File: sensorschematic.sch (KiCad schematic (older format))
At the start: 6 parts, among them J1 Conn_01x03_Male, U1 LM35DZ_NOPB

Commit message: Updated Parts
Updated parts to components that are available for order rather than obsolete, out-of-stock, or non-real components.
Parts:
- removed C1, C2: C, symbol pspice:C
- removed C3: 1uF, symbol pspice:C
- removed R1: 75, symbol Device:R_US
- added C1: CL21B474KOFNNNE, CAP_CL21_SAM, symbol CL21B474KOFNNNE:CL21B474KOFNNNE
- added C2: 04025C101KAT2A, 0402_AVX, symbol 04025C101KAT2A:04025C101KAT2A
- added C3: CL05A105KO5NNNC, CAP_CL05_SAM, symbol CL05A105KO5NNNC:CL05A105KO5NNNC
- added R1: CR0603-FX-75R0ELF, BO_CR0603, symbol CR0603-FX-75R0ELF:CR0603-FX-75R0ELF
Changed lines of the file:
@@
 $EndDescr
-$Comp
-L pspice:C C1
-U 1 1 60F31FB8
-P 2000 3300
-AR Path="/5EA98F1B/60F31FB8" Ref="C1"  Part="1"
-AR Path="/60B9480C/60F31FB8" Ref="C4"  Part="1"
-AR Path="/60B94B7E/60F31FB8" Ref="C7"  Part="1"
-AR Path="/60B95D06/60F31FB8" Ref="C10"  Part="1"
-AR Path="/60B95D0B/60F31FB8" Ref="C13"  Part="1"
-AR Path="/60B95D10/60F31FB8" Ref="C16"  Part="1"
-AR Path="/60B99A53/60F31FB8" Ref="C19"  Part="1"
-AR Path="/60B99A58/60F31FB8" Ref="C22"  Part="1"
-AR Path="/60B99A5D/60F31FB8" Ref="C25"  Part="1"
-AR Path="/60B99A62/60F31FB8" Ref="C28"  Part="1"
-AR Path="/60B99A67/60F31FB8" Ref="C31"  Part="1"
-AR Path="/60B99A6C/60F31FB8" Ref="C34"  Part="1"
-F 0 "C34" H 2178 3391 50  0000 L CNN
-F 1 "C" H 2178 3346 50  0001 L CNN
-F 2 "" H 2000 3300 50  0001 C CNN
-F 3 "~" H 2000 3300 50  0001 C CNN
-F 4 "C" H 2000 3300 50  0001 C CNN "Spice_Primitive"
-F 5 ".47u" H 2178 3300 50  0000 L CNN "Spice_Model"
-F 6 "Y" H 2000 3300 50  0001 C CNN "Spice_Netlist_Enabled"
-F 7 "16V" H 2178 3209 50  0000 L CNN "Vmax"
-	1    2000 3300
-	1    0    0    -1
-$EndComp
-$Comp
-L pspice:C C2
-U 1 1 60F3306C
-P 2600 3300
-AR Path="/5EA98F1B/60F3306C" Ref="C2"  Part="1"
-AR Path="/60B9480C/60F3306C" Ref="C5"  Part="1"
-AR Path="/60B94B7E/60F3306C" Ref="C8"  Part="1"
-AR Path="/60B95D06/60F3306C" Ref="C11"  Part="1"
-AR Path="/60B95D0B/60F3306C" Ref="C14"  Part="1"
-AR Path="/60B95D10/60F3306C" Ref="C17"  Part="1"
-AR Path="/60B99A53/60F3306C" Ref="C20"  Part="1"
-AR Path="/60B99A58/60F3306C" Ref="C23"  Part="1"
-AR Path="/60B99A5D/60F3306C" Ref="C26"  Part="1"
-AR Path="/60B99A62/60F3306C" Ref="C29"  Part="1"
-AR Path="/60B99A67/60F3306C" Ref="C32"  Part="1"
-AR Path="/60B99A6C/60F3306C" Ref="C35"  Part="1"
-F 0 "C35" H 2778 3391 50  0000 L CNN
-F 1 "C" H 2778 3300 50  0001 L CNN
-F 2 "" H 2600 3300 50  0001 C CNN
-F 3 "~" H 2600 3300 50  0001 C CNN
-F 4 "C" H 2600 3300 50  0001 C CNN "Spice_Primitive"
-F 5 "100p" H 2778 3300 50  0000 L CNN "Spice_Model"
-F 6 "Y" H 2600 3300 50  0001 C CNN "Spice_Netlist_Enabled"
-F 7 "50V" H 2778 3209 50  0000 L CNN "Vmax"
-	1    2600 3300
-	1    0    0    -1
-$EndComp
-$Comp
-L pspice:C C3
-U 1 1 60F35AED
-P 5100 4500
-AR Path="/5EA98F1B/60F35AED" Ref="C3"  Part="1"
-AR Path="/60B9480C/60F35AED" Ref="C6"  Part="1"
-AR Path="/60B94B7E/60F35AED" Ref="C9"  Part="1"
-AR Path="/60B95D06/60F35AED" Ref="C12"  Part="1"
-AR Path="/60B95D0B/60F35AED" Ref="C15"  Part="1"
-AR Path="/60B95D10/60F35AED" Ref="C18"  Part="1"
-AR Path="/60B99A53/60F35AED" Ref="C21"  Part="1"
-AR Path="/60B99A58/60F35AED" Ref="C24"  Part="1"
-AR Path="/60B99A5D/60F35AED" Ref="C27"  Part="1"
-AR Path="/60B99A62/60F35AED" Ref="C30"  Part="1"
-AR Path="/60B99A67/60F35AED" Ref="C33"  Part="1"
-AR Path="/60B99A6C/60F35AED" Ref="C36"  Part="1"
-F 0 "C36" H 5278 4546 50  0000 L CNN
-F 1 "1uF" H 5278 4455 50  0001 L CNN
-F 2 "" H 5100 4500 50  0001 C CNN
-F 3 "~" H 5100 4500 50  0001 C CNN
-F 4 "C" H 5100 4500 50  0001 C CNN "Spice_Primitive"
-F 5 "1u" H 5278 4455 50  0000 L CNN "Spice_Model"
-F 6 "Y" H 5100 4500 50  0001 C CNN "Spice_Netlist_Enabled"
-	1    5100 4500
-	1    0    0    -1
-$EndComp
-$Comp
-L Device:R_US R1
-U 1 1 60F37AD0
-P 5100 3900
-AR Path="/5EA98F1B/60F37AD0" Ref="R1"  Part="1"
-AR Path="/60B9480C/60F37AD0" Ref="R2"  Part="1"
-AR Path="/60B94B7E/60F37AD0" Ref="R3"  Part="1"
-AR Path="/60B95D06/60F37AD0" Ref="R4"  Part="1"
-AR Path="/60B95D0B/60F37AD0" Ref="R5"  Part="1"
-AR Path="/60B95D10/60F37AD0" Ref="R6"  Part="1"
-AR Path="/60B99A53/60F37AD0" Ref="R7"  Part="1"
-AR Path="/60B99A58/60F37AD0" Ref="R8"  Part="1"
-AR Path="/60B99A5D/60F37AD0" Ref="R9"  Part="1"
-AR Path="/60B99A62/60F37AD0" Ref="R10"  Part="1"
-AR Path="/60B99A67/60F37AD0" Ref="R11"  Part="1"
-AR Path="/60B99A6C/60F37AD0" Ref="R12"  Part="1"
-F 0 "R12" H 5168 3946 50  0000 L CNN
-F 1 "75" H 5168 3855 50  0001 L CNN
-F 2 "" V 5140 3890 50  0001 C CNN
-F 3 "~" H 5100 3900 50  0001 C CNN
-F 4 "R" H 5100 3900 50  0001 C CNN "Spice_Primitive"
-F 5 "75" H 5168 3855 50  0000 L CNN "Spice_Model"
-F 6 "Y" H 5100 3900 50  0001 C CNN "Spice_Netlist_Enabled"
-	1    5100 3900
-	1    0    0    -1
-$EndComp
 $Comp
 L Connector:Conn_01x03_Male J1
@@
 	6200 3200 5900 3200
 Wire Wire Line
-	2600 2750 2600 3050
-Wire Wire Line
 	2600 2750 2000 2750
 Wire Wire Line
-	2000 2750 2000 3050
-Wire Wire Line
-	6200 3300 5100 3300
-Wire Wire Line
-	5100 3300 5100 3750
-Wire Wire Line
 	5900 2750 5900 3200
-Wire Wire Line
-	5100 4050 5100 4250
 $Comp
 L power:GNDREF #PWR01
@@
 Wire Wire Line
 	6000 3400 6000 3800
-Wire Wire Line
-	5100 4750 5100 4950
-Wire Wire Line
-	2600 3550 2600 3750
-Wire Wire Line
-	2000 3550 2000 3800
 Text Label 5900 2750 0    50   ~ 0
 Vs
@@
 Wire Wire Line
 	4900 3500 4900 3300
-Wire Wire Line
-	4900 3300 5100 3300
-Connection ~ 5100 3300
 Wire Wire Line
 	4100 4250 4100 4550
@@
 	1    0    0    -1
 $EndComp
+$Comp
+L CL05A105KO5NNNC:CL05A105KO5NNNC C3
+U 1 1 6141E476
+P 5100 4350
+AR Path="/5EA98F1B/6141E476" Ref="C3"  Part="1"
+AR Path="/60B9480C/6141E476" Ref="C6"  Part="1"
+AR Path="/60B94B7E/6141E476" Ref="C9"  Part="1"
+AR Path="/60B95D06/6141E476" Ref="C12"  Part="1"
+AR Path="/60B95D0B/6141E476" Ref="C15"  Part="1"
+AR Path="/60B95D10/6141E476" Ref="C18"  Part="1"
+AR Path="/60B99A53/6141E476" Ref="C21"  Part="1"
+AR Path="/60B99A58/6141E476" Ref="C24"  Part="1"
+AR Path="/60B99A5D/6141E476" Ref="C27"  Part="1"
+AR Path="/60B99A62/6141E476" Ref="C30"  Part="1"
+AR Path="/60B99A67/6141E476" Ref="C33"  Part="1"
+AR Path="/60B99A6C/6141E476" Ref="C36"  Part="1"
+F 0 "C36" V 5197 4454 60  0000 L CNN
+F 1 "CL05A105KO5NNNC" V 5303 4454 60  0000 L CNN
+F 2 "CAP_CL05_SAM" H 5250 3990 60  0001 C CNN
+F 3 "" H 5100 4350 60  0000 C CNN
+	1    5100 4350
+	0    1    1    0
+$EndComp
+Wire Wire Line
+	5100 4650 5100 4950
+$Comp
+L 04025C101KAT2A:04025C101KAT2A C2
+U 1 1 61420529
+P 2600 3150
+AR Path="/5EA98F1B/61420529" Ref="C2"  Part="1"
+AR Path="/60B9480C/61420529" Ref="C5"  Part="1"
+AR Path="/60B94B7E/61420529" Ref="C8"  Part="1"
+AR Path="/60B95D06/61420529" Ref="C11"  Part="1"
+AR Path="/60B95D0B/61420529" Ref="C14"  Part="1"
+AR Path="/60B95D10/61420529" Ref="C17"  Part="1"
+AR Path="/60B99A53/61420529" Ref="C20"  Part="1"
+AR Path="/60B99A58/61420529" Ref="C23"  Part="1"
+AR Path="/60B99A5D/61420529" Ref="C26"  Part="1"
+AR Path="/60B99A62/61420529" Ref="C29"  Part="1"
+AR Path="/60B99A67/61420529" Ref="C32"  Part="1"
+AR Path="/60B99A6C/61420529" Ref="C35"  Part="1"
+F 0 "C35" V 2697 3254 60  0000 L CNN
+F 1 "04025C101KAT2A" V 2803 3254 60  0000 L CNN
+F 2 "0402_AVX" H 2750 2790 60  0001 C CNN
+F 3 "" H 2600 3150 60  0000 C CNN
+	1    2600 3150
+	0    1    1    0
+$EndComp
+Wire Wire Line
+	2600 2750 2600 3150
+Wire Wire Line
+	2600 3450 2600 3750
+$Comp
+L CL21B474KOFNNNE:CL21B474KOFNNNE C1
+U 1 1 614228FD
+P 2000 3150
+AR Path="/5EA98F1B/614228FD" Ref="C1"  Part="1"
+AR Path="/60B9480C/614228FD" Ref="C4"  Part="1"
+AR Path="/60B94B7E/614228FD" Ref="C7"  Part="1"
+AR Path="/60B95D06/614228FD" Ref="C10"  Part="1"
+AR Path="/60B95D0B/614228FD" Ref="C13"  Part="1"
+AR Path="/60B95D10/614228FD" Ref="C16"  Part="1"
+AR Path="/60B99A53/614228FD" Ref="C19"  Part="1"
+AR Path="/60B99A58/614228FD" Ref="C22"  Part="1"
+AR Path="/60B99A5D/614228FD" Ref="C25"  Part="1"
+AR Path="/60B99A62/614228FD" Ref="C28"  Part="1"
+AR Path="/60B99A67/614228FD" Ref="C31"  Part="1"
+AR Path="/60B99A6C/614228FD" Ref="C34"  Part="1"
+F 0 "C34" V 2097 3254 60  0000 L CNN
+F 1 "CL21B474KOFNNNE" V 2203 3254 60  0000 L CNN
+F 2 "CAP_CL21_SAM" H 2150 2790 60  0001 C CNN
+F 3 "" H 2000 3150 60  0000 C CNN
+	1    2000 3150
+	0    1    1    0
+$EndComp
+Wire Wire Line
+	2000 2750 2000 3150
+Wire Wire Line
+	2000 3450 2000 3800
+$Comp
+L CR0603-FX-75R0ELF:CR0603-FX-75R0ELF R1
+U 1 1 61424F1B
+P 5100 3650
+AR Path="/5EA98F1B/61424F1B" Ref="R1"  Part="1"
+AR Path="/60B9480C/61424F1B" Ref="R2"  Part="1"
+AR Path="/60B94B7E/61424F1B" Ref="R3"  Part="1"
+AR Path="/60B95D06/61424F1B" Ref="R4"  Part="1"
+AR Path="/60B95D0B/61424F1B" Ref="R5"  Part="1"
+AR Path="/60B95D10/61424F1B" Ref="R6"  Part="1"
+AR Path="/60B99A53/61424F1B" Ref="R7"  Part="1"
+AR Path="/60B99A58/61424F1B" Ref="R8"  Part="1"
+AR Path="/60B99A5D/61424F1B" Ref="R9"  Part="1"
+AR Path="/60B99A62/61424F1B" Ref="R10"  Part="1"
+AR Path="/60B99A67/61424F1B" Ref="R11"  Part="1"
+AR Path="/60B99A6C/61424F1B" Ref="R12"  Part="1"
+F 0 "R12" V 5297 3729 60  0000 L CNN
+F 1 "CR0603-FX-75R0ELF" V 5403 3729 60  0000 L CNN
+F 2 "BO_CR0603" H 5350 3315 60  0001 C CNN
+F 3 "" H 5100 3650 60  0000 C CNN
+	1    5100 3650
+	0    1    1    0
+$EndComp
+Wire Wire Line
+	4900 3300 5100 3300
+Wire Wire Line
+	5100 3650 5100 3300
+Connection ~ 5100 3300
+Wire Wire Line
+	5100 3300 6200 3300
+Wire Wire Line
+	5100 4350 5100 4150
 $EndSCHEMATC

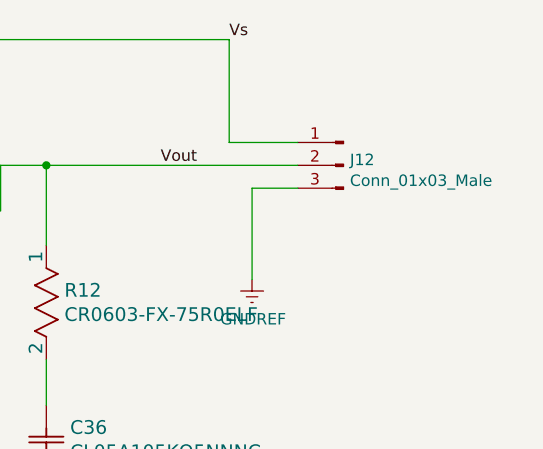
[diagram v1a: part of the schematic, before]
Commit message: Finished Component Selection
Finished Component selection in schematic and BoM. Ready to design PCB
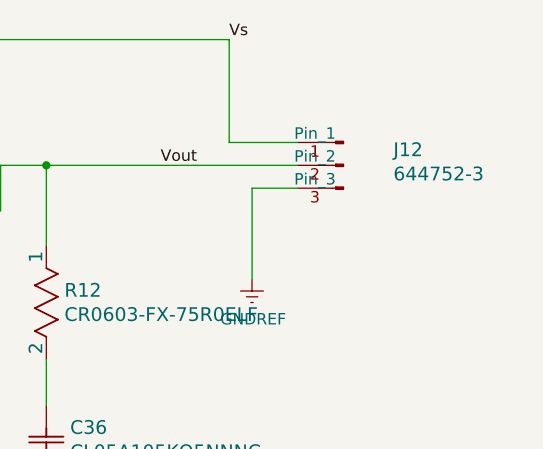
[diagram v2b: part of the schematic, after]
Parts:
- removed J1: Conn_01x03_Male, symbol Connector:Conn_01x03_Male
- added J1: 644752-3, 644752-3_TYC, symbol 644752-3:644752-3
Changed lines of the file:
@@
 Comment4 ""
 $EndDescr
-$Comp
-L Connector:Conn_01x03_Male J1
-U 1 1 60F387FB
-P 6400 3300
-AR Path="/5EA98F1B/60F387FB" Ref="J1"  Part="1"
-AR Path="/60B9480C/60F387FB" Ref="J2"  Part="1"
-AR Path="/60B94B7E/60F387FB" Ref="J3"  Part="1"
-AR Path="/60B95D06/60F387FB" Ref="J4"  Part="1"
-AR Path="/60B95D0B/60F387FB" Ref="J5"  Part="1"
-AR Path="/60B95D10/60F387FB" Ref="J6"  Part="1"
-AR Path="/60B99A53/60F387FB" Ref="J7"  Part="1"
-AR Path="/60B99A58/60F387FB" Ref="J8"  Part="1"
-AR Path="/60B99A5D/60F387FB" Ref="J9"  Part="1"
-AR Path="/60B99A62/60F387FB" Ref="J10"  Part="1"
-AR Path="/60B99A67/60F387FB" Ref="J11"  Part="1"
-AR Path="/60B99A6C/60F387FB" Ref="J12"  Part="1"
-F 0 "J12" H 6372 3324 50  0000 R CNN
-F 1 "Conn_01x03_Male" H 6372 3233 50  0000 R CNN
-F 2 "" H 6400 3300 50  0001 C CNN
-F 3 "~" H 6400 3300 50  0001 C CNN
-	1    6400 3300
-	-1   0    0    -1
-$EndComp
 Wire Wire Line
 	6200 3200 5900 3200
@@
 Wire Wire Line
 	5100 4350 5100 4150
+$Comp
+L 644752-3:644752-3 J1
+U 1 1 6196DD58
+P 5550 3450
+AR Path="/5EA98F1B/6196DD58" Ref="J1"  Part="1"
+AR Path="/60B9480C/6196DD58" Ref="J2"  Part="1"
+AR Path="/60B94B7E/6196DD58" Ref="J3"  Part="1"
+AR Path="/60B95D06/6196DD58" Ref="J4"  Part="1"
+AR Path="/60B95D0B/6196DD58" Ref="J5"  Part="1"
+AR Path="/60B95D10/6196DD58" Ref="J6"  Part="1"
+AR Path="/60B99A53/6196DD58" Ref="J7"  Part="1"
+AR Path="/60B99A58/6196DD58" Ref="J8"  Part="1"
+AR Path="/60B99A5D/6196DD58" Ref="J9"  Part="1"
+AR Path="/60B99A62/6196DD58" Ref="J10"  Part="1"
+AR Path="/60B99A67/6196DD58" Ref="J11"  Part="1"
+AR Path="/60B99A6C/6196DD58" Ref="J12"  Part="1"
+F 0 "J12" H 4482 3668 60  0000 R CNN
+F 1 "644752-3" H 4482 3562 60  0000 R CNN
+F 2 "644752-3_TYC" H 4750 3790 60  0001 C CNN
+F 3 "" H 5550 3450 60  0000 C CNN
+	1    5550 3450
+	-1   0    0    -1
+$EndComp
 $EndSCHEMATC
